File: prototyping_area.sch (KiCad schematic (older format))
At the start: 22 parts, among them J1 GND_rail, J10 Conn_01x01_Female, J11 Conn_01x01_Female, J12 Conn_01x01_Female, J13 Conn_01x01_Female, J14 Conn_01x01_Female, J15 Conn_01x01_Female, J16 Conn_01x01_Female, J17 Conn_01x01_Female, J18 Conn_01x01_Female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

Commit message: Added associations for new symbols.
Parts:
- J1, J6: footprint (none) -> Connector_PinHeader_2.54mm:PinHeader_1x05_P2.54mm_Vertical
- J10, J11, J12, J13, J14, J15, J16, J17, J18, J19, J20, J21, J22, J23, J24, J25, J26, J7, J8, J9: footprint (none) -> Connector_Pin:Pin_D1.0mm_L10.0mm_LooseFit
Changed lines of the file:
@@
 F 0 "J1" H 3272 2730 50  0000 R CNN
 F 1 "GND_rail" H 3272 2821 50  0000 R CNN
-F 2 "" H 3300 2800 50  0001 C CNN
+F 2 "Connector_PinHeader_2.54mm:PinHeader_1x05_P2.54mm_Vertical" H 3300 2800 50  0001 C CNN
 F 3 "~" H 3300 2800 50  0001 C CNN
 	1    3300 2800
@@
 F 0 "J6" H 3273 3580 50  0000 R CNN
 F 1 "5V_Rail" H 3273 3671 50  0000 R CNN
-F 2 "" H 3300 3650 50  0001 C CNN
+F 2 "Connector_PinHeader_2.54mm:PinHeader_1x05_P2.54mm_Vertical" H 3300 3650 50  0001 C CNN
 F 3 "~" H 3300 3650 50  0001 C CNN
 	1    3300 3650
@@
 F 0 "J7" H 4300 2600 50  0000 L CNN
 F 1 "Conn_01x01_Female" H 4450 2600 50  0001 L CNN
-F 2 "" H 4450 2650 50  0001 C CNN
+F 2 "Connector_Pin:Pin_D1.0mm_L10.0mm_LooseFit" H 4450 2650 50  0001 C CNN
 F 3 "~" H 4450 2650 50  0001 C CNN
 	1    4450 2650
@@
 F 0 "J8" H 4300 2850 50  0000 L CNN
 F 1 "Conn_01x01_Female" H 4450 2850 50  0001 L CNN
-F 2 "" H 4450 2900 50  0001 C CNN
+F 2 "Connector_Pin:Pin_D1.0mm_L10.0mm_LooseFit" H 4450 2900 50  0001 C CNN
 F 3 "~" H 4450 2900 50  0001 C CNN
 	1    4450 2900
@@
 F 0 "J9" H 4300 3100 50  0000 L CNN
 F 1 "Conn_01x01_Female" H 4450 3100 50  0001 L CNN
-F 2 "" H 4450 3150 50  0001 C CNN
+F 2 "Connector_Pin:Pin_D1.0mm_L10.0mm_LooseFit" H 4450 3150 50  0001 C CNN
 F 3 "~" H 4450 3150 50  0001 C CNN
 	1    4450 3150
@@
 F 0 "J10" H 4300 3350 50  0000 L CNN
 F 1 "Conn_01x01_Female" H 4450 3350 50  0001 L CNN
-F 2 "" H 4450 3400 50  0001 C CNN
+F 2 "Connector_Pin:Pin_D1.0mm_L10.0mm_LooseFit" H 4450 3400 50  0001 C CNN
 F 3 "~" H 4450 3400 50  0001 C CNN
 	1    4450 3400
@@
 F 0 "J11" H 4300 3600 50  0000 L CNN
 F 1 "Conn_01x01_Female" H 4450 3600 50  0001 L CNN
-F 2 "" H 4450 3650 50  0001 C CNN
+F 2 "Connector_Pin:Pin_D1.0mm_L10.0mm_LooseFit" H 4450 3650 50  0001 C CNN
 F 3 "~" H 4450 3650 50  0001 C CNN
 	1    4450 3650
@@
 F 0 "J12" H 4800 2600 50  0000 L CNN
 F 1 "Conn_01x01_Female" H 4950 2600 50  0001 L CNN
-F 2 "" H 4950 2650 50  0001 C CNN
+F 2 "Connector_Pin:Pin_D1.0mm_L10.0mm_LooseFit" H 4950 2650 50  0001 C CNN
 F 3 "~" H 4950 2650 50  0001 C CNN
 	1    4950 2650
@@
 F 0 "J13" H 4800 2850 50  0000 L CNN
 F 1 "Conn_01x01_Female" H 4950 2850 50  0001 L CNN
-F 2 "" H 4950 2900 50  0001 C CNN
+F 2 "Connector_Pin:Pin_D1.0mm_L10.0mm_LooseFit" H 4950 2900 50  0001 C CNN
 F 3 "~" H 4950 2900 50  0001 C CNN
 	1    4950 2900
@@
 F 0 "J14" H 4800 3100 50  0000 L CNN
 F 1 "Conn_01x01_Female" H 4950 3100 50  0001 L CNN
-F 2 "" H 4950 3150 50  0001 C CNN
+F 2 "Connector_Pin:Pin_D1.0mm_L10.0mm_LooseFit" H 4950 3150 50  0001 C CNN
 F 3 "~" H 4950 3150 50  0001 C CNN
 	1    4950 3150
@@
 F 0 "J15" H 4800 3350 50  0000 L CNN
 F 1 "Conn_01x01_Female" H 4950 3350 50  0001 L CNN
-F 2 "" H 4950 3400 50  0001 C CNN
+F 2 "Connector_Pin:Pin_D1.0mm_L10.0mm_LooseFit" H 4950 3400 50  0001 C CNN
 F 3 "~" H 4950 3400 50  0001 C CNN
 	1    4950 3400
@@
 F 0 "J16" H 4800 3600 50  0000 L CNN
 F 1 "Conn_01x01_Female" H 4950 3600 50  0001 L CNN
-F 2 "" H 4950 3650 50  0001 C CNN
+F 2 "Connector_Pin:Pin_D1.0mm_L10.0mm_LooseFit" H 4950 3650 50  0001 C CNN
 F 3 "~" H 4950 3650 50  0001 C CNN
 	1    4950 3650
@@
 F 0 "J17" H 5300 2600 50  0000 L CNN
 F 1 "Conn_01x01_Female" H 5450 2600 50  0001 L CNN
-F 2 "" H 5450 2650 50  0001 C CNN
+F 2 "Connector_Pin:Pin_D1.0mm_L10.0mm_LooseFit" H 5450 2650 50  0001 C CNN
 F 3 "~" H 5450 2650 50  0001 C CNN
 	1    5450 2650
@@
 F 0 "J18" H 5300 2850 50  0000 L CNN
 F 1 "Conn_01x01_Female" H 5450 2850 50  0001 L CNN
-F 2 "" H 5450 2900 50  0001 C CNN
+F 2 "Connector_Pin:Pin_D1.0mm_L10.0mm_LooseFit" H 5450 2900 50  0001 C CNN
 F 3 "~" H 5450 2900 50  0001 C CNN
 	1    5450 2900
@@
 F 0 "J19" H 5300 3100 50  0000 L CNN
 F 1 "Conn_01x01_Female" H 5450 3100 50  0001 L CNN
-F 2 "" H 5450 3150 50  0001 C CNN
+F 2 "Connector_Pin:Pin_D1.0mm_L10.0mm_LooseFit" H 5450 3150 50  0001 C CNN
 F 3 "~" H 5450 3150 50  0001 C CNN
 	1    5450 3150
@@
 F 0 "J20" H 5300 3350 50  0000 L CNN
 F 1 "Conn_01x01_Female" H 5450 3350 50  0001 L CNN
-F 2 "" H 5450 3400 50  0001 C CNN
+F 2 "Connector_Pin:Pin_D1.0mm_L10.0mm_LooseFit" H 5450 3400 50  0001 C CNN
 F 3 "~" H 5450 3400 50  0001 C CNN
 	1    5450 3400
@@
 F 0 "J21" H 5300 3600 50  0000 L CNN
 F 1 "Conn_01x01_Female" H 5450 3600 50  0001 L CNN
-F 2 "" H 5450 3650 50  0001 C CNN
+F 2 "Connector_Pin:Pin_D1.0mm_L10.0mm_LooseFit" H 5450 3650 50  0001 C CNN
 F 3 "~" H 5450 3650 50  0001 C CNN
 	1    5450 3650
@@
 F 0 "J22" H 5800 2600 50  0000 L CNN
 F 1 "Conn_01x01_Female" H 5950 2600 50  0001 L CNN
-F 2 "" H 5950 2650 50  0001 C CNN
+F 2 "Connector_Pin:Pin_D1.0mm_L10.0mm_LooseFit" H 5950 2650 50  0001 C CNN
 F 3 "~" H 5950 2650 50  0001 C CNN
 	1    5950 2650
@@
 F 0 "J23" H 5800 2850 50  0000 L CNN
 F 1 "Conn_01x01_Female" H 5950 2850 50  0001 L CNN
-F 2 "" H 5950 2900 50  0001 C CNN
+F 2 "Connector_Pin:Pin_D1.0mm_L10.0mm_LooseFit" H 5950 2900 50  0001 C CNN
 F 3 "~" H 5950 2900 50  0001 C CNN
 	1    5950 2900
@@
 F 0 "J24" H 5800 3100 50  0000 L CNN
 F 1 "Conn_01x01_Female" H 5950 3100 50  0001 L CNN
-F 2 "" H 5950 3150 50  0001 C CNN
+F 2 "Connector_Pin:Pin_D1.0mm_L10.0mm_LooseFit" H 5950 3150 50  0001 C CNN
 F 3 "~" H 5950 3150 50  0001 C CNN
 	1    5950 3150
@@
 F 0 "J25" H 5800 3350 50  0000 L CNN
 F 1 "Conn_01x01_Female" H 5950 3350 50  0001 L CNN
-F 2 "" H 5950 3400 50  0001 C CNN
+F 2 "Connector_Pin:Pin_D1.0mm_L10.0mm_LooseFit" H 5950 3400 50  0001 C CNN
 F 3 "~" H 5950 3400 50  0001 C CNN
 	1    5950 3400
@@
 F 0 "J26" H 5800 3600 50  0000 L CNN
 F 1 "Conn_01x01_Female" H 5950 3600 50  0001 L CNN
-F 2 "" H 5950 3650 50  0001 C CNN
+F 2 "Connector_Pin:Pin_D1.0mm_L10.0mm_LooseFit" H 5950 3650 50  0001 C CNN
 F 3 "~" H 5950 3650 50  0001 C CNN
 	1    5950 3650

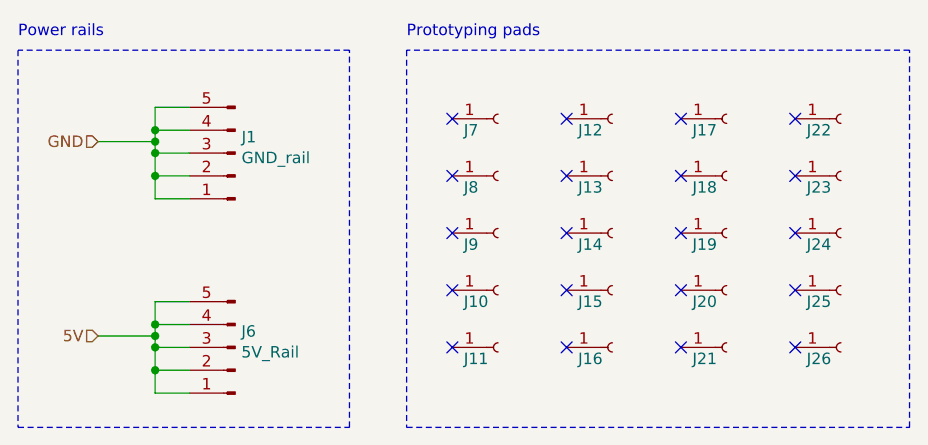
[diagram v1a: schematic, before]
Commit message: Adjusted designators, units etc as per Larry's feedback.
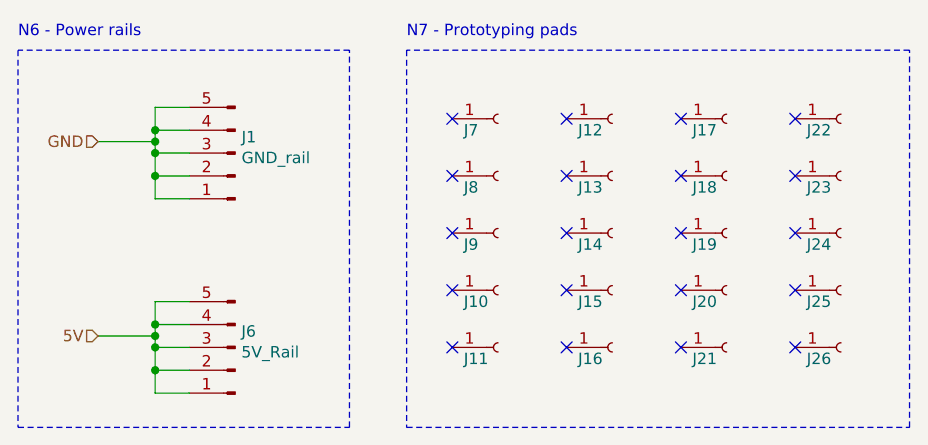
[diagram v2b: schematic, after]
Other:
- note added: "N6 - Power rails"
- note added: "N7 - Prototyping pads"
- note removed: "Power rails"
- note removed: "Prototyping pads"
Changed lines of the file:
@@
 	6250 2350 4050 2350
 Text Notes 2350 2300 0    50   ~ 0
-Power rails
+N6 - Power rails
 Text Notes 4050 2300 0    50   ~ 0
-Prototyping pads
+N7 - Prototyping pads
 $EndSCHEMATC
